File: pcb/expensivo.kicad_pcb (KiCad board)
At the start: 2 copper layers, 132.5 x 95.1 mm, 42 parts, among them K1 MX, K10 MX, K11 MX, K12 MX, K13 MX, K14 MX, K15 MX, K16 MX, K17 MX, K18 MX, K2 MX, K3 MX, K4 MX, K5 MX, K6 MX, K7 MX, K8 MX, K9 MX, SW1 PCM12SMTR, SW2 PCM12SMTR, SW3 RESET, SW4 RESET, U1 nice!nano v2

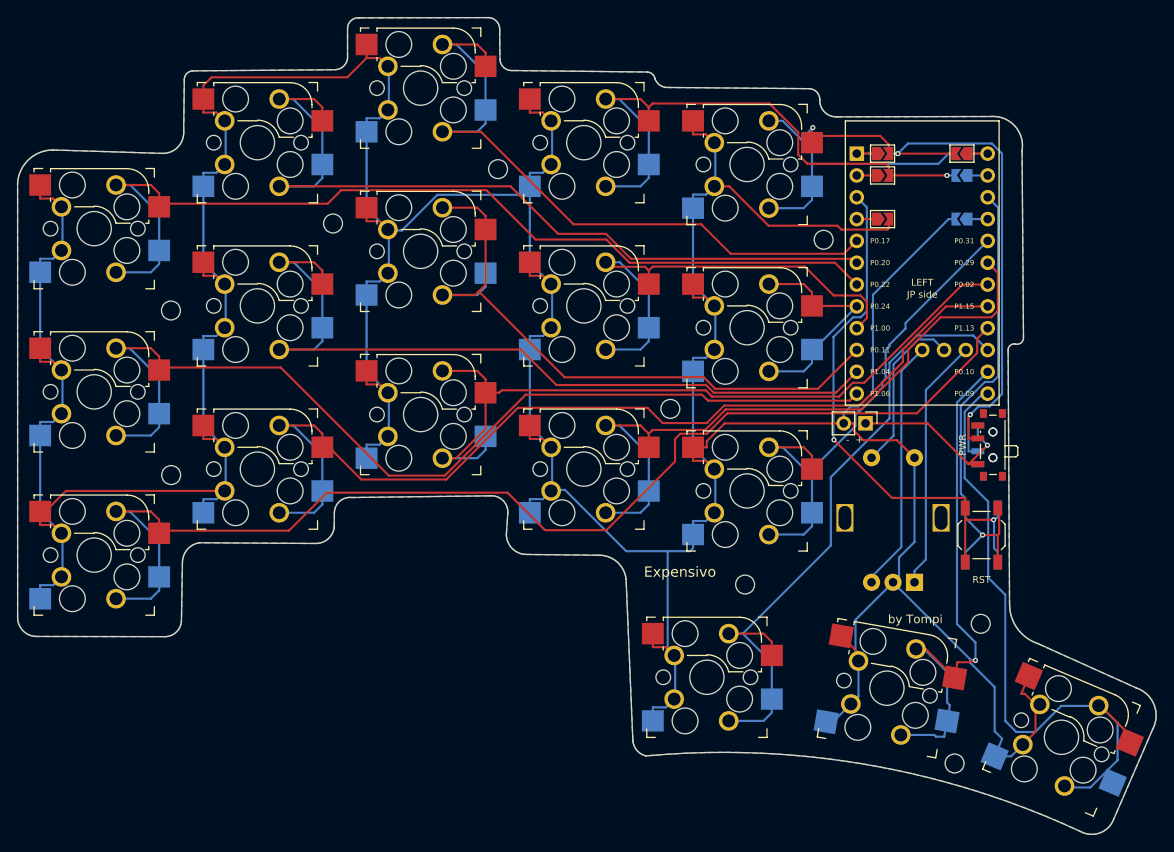
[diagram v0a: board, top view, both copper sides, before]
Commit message: Trim outline, add schematic and 3D-printed case
PCB: outline generated to hug the keys (edge under the keycaps, straight
along the nice!nano, bottom mounting hole dropped, outer thumb socket
turned so its pads face inwards), Impact logo as exposed copper, nano USB
end overhanging the edge.

Schematic: generated from the PCB's parts and nets by
scripts/gen_schematic.py; build.sh checks ERC and schematic parity.

Case: OpenSCAD case adapted from the cheapino, with geometry generated
from the PCB (scripts/gen_case.py): flat top frames, bottom plates, and
optional magnetic covers over the nice!nano with room for the battery.

Co-Authored-By: Claude Opus 5.5 <noreply@anthropic.com>
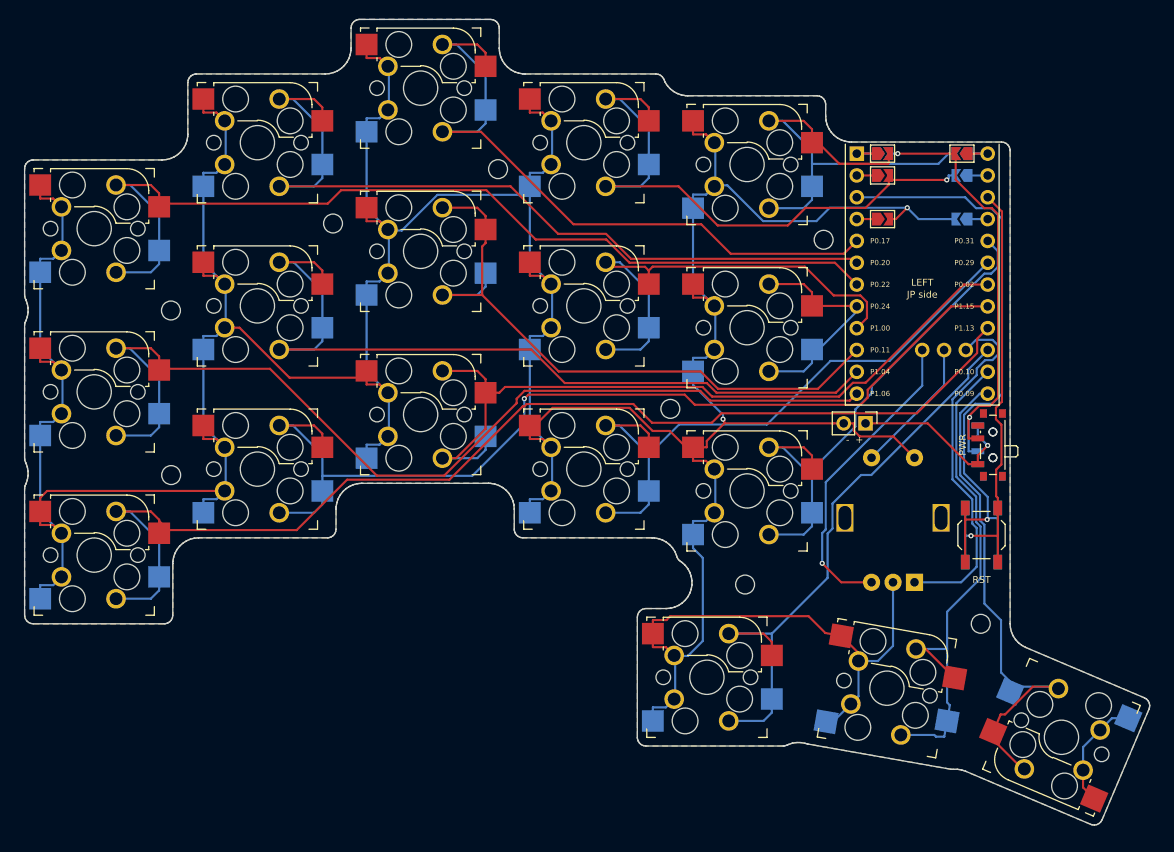
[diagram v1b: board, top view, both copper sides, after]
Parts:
- removed H6: MountingHole_2.2mm_M2, MountingHole:MountingHole_2.2mm_M2
- BT1: footprint PinHeader_1x02_P2.54mm_Vertical -> Connector_PinHeader_2.54mm:PinHeader_1x02_P2.54mm_Vertical
- ENC1: footprint RotaryEncoder_Alps_EC11E-Switch_Vertical_H20mm -> Rotary_Encoder:RotaryEncoder_Alps_EC11E-Switch_Vertical_H20mm
- JP1, JP2, JP3, JP4: value SolderJumper-2_P1.3mm_Open_TrianglePad1.0x1.5mm -> front; footprint SolderJumper-2_P1.3mm_Open_TrianglePad1.0x1.5mm -> Jumper:SolderJumper-2_P1.3mm_Open_TrianglePad1.0x1.5mm
- JP5, JP6, JP7, JP8: value SolderJumper-2_P1.3mm_Open_TrianglePad1.0x1.5mm -> back; footprint SolderJumper-2_P1.3mm_Open_TrianglePad1.0x1.5mm -> Jumper:SolderJumper-2_P1.3mm_Open_TrianglePad1.0x1.5mm
- SW1, SW2: footprint SW_SPDT_PCM12 -> Button_Switch_SMD:SW_SPDT_PCM12
- SW3, SW4: footprint SW_SPST_TL3342 -> Button_Switch_SMD:SW_SPST_TL3342
- turned K16 to 157 degrees
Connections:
- SW1 pad 3: (no net) -> unconnected-(SW1-C-Pad3)
- SW2 pad 3: (no net) -> unconnected-(SW2-C-Pad3)
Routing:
- net GND: track 608.3 -> 570.1 mm, vias 0 -> 2
- net KEY_K16: track 75.0 -> 60.9 mm
- net ENC_A: track 29.5 -> 42.1 mm
- net RAW: track 62.9 -> 51.8 mm
- net RST_A: track 66.6 -> 73.4 mm, vias 2 -> 1
- net ENC_B: track 29.5 -> 36.3 mm, vias 0 -> 1
- net KEY_K18: track 76.7 -> 70.8 mm
- net KEY_K6: track 78.1 -> 73.3 mm
- net KEY_K4: track 66.1 -> 70.7 mm
- net KEY_K1: track 49.0 -> 53.2 mm, vias 1 -> 0
- net ENC_S: track 19.5 -> 16.0 mm
- net KEY_K15: track 137.0 -> 134.0 mm
- net KEY_K17: track 63.5 -> 61.6 mm, vias 1 -> 0
- net KEY_K3: track 60.4 -> 61.8 mm
- net RST_B: track 55.5 -> 54.1 mm
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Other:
- board size 132.5 x 95.1 mm -> 131 x 93.8 mm

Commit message: Move battery pads, label jumpers, add 3D models, v1, snug USB-C opening
PCB: battery pads stacked beside the nano's corner, clear of the battery
sliding in under the nano; "BRIDGE ALL 4" labels between the power-row
jumpers on each side; "v1" silkscreen and board revision.

3D: KiCad models for the hotswap sockets, MX switches and DSA keycaps
(lib/expensivo.3dshapes, licenses in its README); the nice!nano model is
downloaded by build.sh as it is CC BY-NC-SA.

Case: the nano's USB-C is mid-mount, so the port moved down; the USB end
is now a flat face flush with the receptacle with a snug opening, lower
half in the top frame and upper half in the cover; cover 2 mm lower.

Co-Authored-By: Claude Opus 5.5 <noreply@anthropic.com>
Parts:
- moved BT1 1.97 mm to (157.0, 92.2), turned to 0 degrees
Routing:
- net GND: track 570.1 -> 598.6 mm, vias 2 -> 0
- net KEY_K12: track 113.5 -> 127.8 mm, vias 1 -> 2
- net KEY_K9: track 89.2 -> 102.9 mm, vias 0 -> 1
- net KEY_K1: track 53.2 -> 43.3 mm, vias 0 -> 1
- net RST_A: track 73.4 -> 65.3 mm, vias 1 -> 2
- net ENC_A: track 42.1 -> 34.6 mm
- net KEY_K14: track 116.2 -> 109.5 mm
- net KEY_K6: track 73.3 -> 79.5 mm, vias 0 -> 1
- net KEY_K4: track 70.7 -> 65.7 mm
- net RST_B: track 54.1 -> 58.1 mm
- net KEY_K18: track 70.8 -> 74.6 mm, vias 0 -> 3
- net BAT_P: track 20.5 -> 22.3 mm
- net KEY_K15: track 134.0 -> 132.7 mm
- net KEY_K11: track 95.0 -> 95.7 mm
- net RAW: track 51.8 -> 52.4 mm, vias 2 -> 3
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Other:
- board text added: "+"
- board text added: "-"
- board text added: "ALL 4"
- board text added: "BRIDGE"
- board text added: "LEFT:"
- board text added: "RIGHT:"
- board text added: "v1"
- board text removed: "+ -"
- board text removed: "- +"
- board text removed: "JP side"
